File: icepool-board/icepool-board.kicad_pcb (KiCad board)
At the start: 4 copper layers, 131 parts, among them J1 PWR, J2 PWR_IN, J3 I2C, J4 SWD, J5 8P8C_Shielded, J6 8P8C_Shielded, SW1 B3U-1000P, U1 LD1117S33CTR, U2 LD1117S12CTR, U3 ATSAMD21E, U4 ISL83488/ISL83490, U5 iCE40HX8K-BG121(121-Ball_caBG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, U6 iCE40HX8K-BG121(121-Ball_caBG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, X1 ASV-12.000MHz-L??-50, Y1 16MHz

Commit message: Playing with layout a bit more.
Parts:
- removed L1, L2: FB, Inductor_SMD:L_0805_2012Metric
- removed the R13 at (94.1, 125.0)
- removed the R19 at (96.0, 119.0)
- removed the R6 at (83.1, 123.0)
- removed the R7 at (83.1, 127.0)
- added R1: 0R, Jumper:SolderJumper-2_P1.3mm_Open_TrianglePad1.0x1.5mm, F.Cu at (65.0, 154.0)
- added R11: 10k, Resistor_SMD:R_0805_2012Metric, F.Cu at (89.1, 144.2)
- added R14: 10k, Resistor_SMD:R_0805_2012Metric, F.Cu at (94.1, 143.2)
- added R15: 10k, Resistor_SMD:R_0805_2012Metric, F.Cu at (94.1, 140.2)
- added R21: OMIT, Resistor_SMD:R_0805_2012Metric_Pad1.15x1.40mm_HandSolder, F.Cu at (96.0, 134.2)
- added R4: 10k, Resistor_SMD:R_0805_2012Metric, F.Cu at (50.0, 143.5)
- JP1: moved to F.Cu
- R2: value 10k -> 0R; footprint Resistor_SMD:R_0805_2012Metric -> Jumper:SolderJumper-2_P1.3mm_Open_TrianglePad1.0x1.5mm
- R20: renamed from R18; moved to F.Cu
- moved C26 108.7 mm to (77.0, 113.0)
- moved C22 108.6 mm to (77.0, 119.0), turned to 270 degrees
- moved C23 107.8 mm to (75.0, 119.0), turned to 90 degrees
- moved C25 98.5 mm to (77.0, 115.0)
- moved R7 71.9 mm to (41.0, 158.8), turned to 180 degrees
- moved J3 68.8 mm to (37.0, 156.2), turned to 0 degrees
- moved R6 67.0 mm to (41.0, 156.2), turned to 180 degrees
- moved J1 56.1 mm to (105.4, 90.2), turned to 270 degrees
- moved J2 49.5 mm to (95.2, 92.7), turned to 180 degrees
- moved J5 47.0 mm to (68.6, 90.2), turned to 0 degrees
- moved R2 34.1 mm to (87.0, 154.0)
- moved J4 27.4 mm to (78.0, 102.5)
- moved R17 27.2 mm to (70.0, 106.8)
- moved U4 26.5 mm to (44.5, 102.9)
- moved U5 22.4 mm to (74.2, 116.0)
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- renumbered R11 to R13, R14 to R16, R15 to R17, R16 to R18, R17 to R19, R20 to R22, R21 to R23, R22 to R24, R23 to R25, R24 to R26, R25 to R27, R26 to R28, R27 to R29, R1 to R3, R28 to R30, R29 to R31, R30 to R32, R31 to R33, R3 to R5, R4 to R6, R5 to R7
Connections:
- J1 pad 1: /VPWR -> Net-(J1-Pad1)
- J1 pad 2: Net-(J1-Pad2) -> /VPWR
- J4 pad 6: (no net) -> /TDO
- J4 pad 8: (no net) -> /TDI
- J5 pad 1: /TX+ -> /RX+
- J5 pad 2: /TX- -> /RX-
- J5 pad 3: /RX+ -> /TX+
- J5 pad 4: (no net) -> Net-(J5-Pad4)
- J5 pad 5: (no net) -> Net-(J5-Pad5)
- J5 pad 6: /RX- -> /TX-
- J5 pad 7: (no net) -> Net-(J5-Pad7)
- J5 pad 8: (no net) -> Net-(J5-Pad8)
- J6 pad 1: /TX+ -> /RX+
- J6 pad 2: /TX- -> /RX-
- J6 pad 3: /RX+ -> /TX+
- J6 pad 4: (no net) -> Net-(J6-Pad4)
- J6 pad 5: (no net) -> Net-(J6-Pad5)
- J6 pad 6: /RX- -> /TX-
- J6 pad 7: (no net) -> Net-(J6-Pad7)
- J6 pad 8: (no net) -> Net-(J6-Pad8)
- JP1 pad 1: /RX- -> Net-(JP1-Pad1)
- JP1 pad 2: Net-(JP1-Pad2) -> /RX+
- L3 pad 1: Net-(J1-Pad2) -> Net-(J1-Pad1)
- L4 pad 2: /VDDIN -> +3V3
- R10 pad 1: /CRESET_B -> /~READY_ANY
- R12 pad 1: GND -> /CRESET_B
- R12 pad 2: /MOSI -> +3V3
- R2 pad 1: +3V3 -> Net-(R2-Pad1)
- R2 pad 2: /~RESET -> VCC
- R20 pad 1: /RX+ -> Net-(JP1-Pad1)
- R20 pad 2: Net-(JP1-Pad2) -> /RX-
- R3 pad 1: Net-(L2-Pad1) -> +1V2
- R8 pad 1: /~READY_ANY -> /~WE
- R9 pad 1: /~READY_ANY -> /~GS
- U1 pad 2: Net-(L1-Pad1) -> +3V3
- U1 pad 3: VCC -> Net-(R1-Pad1)
- U1 pad 4: Net-(L1-Pad1) -> +3V3
- U2 pad 2: Net-(L2-Pad1) -> +1V2
- U2 pad 3: VCC -> Net-(R2-Pad1)
- U2 pad 4: Net-(L2-Pad1) -> +1V2
- U3 pad 13: (no net) -> Net-(U3-Pad13)
- U3 pad 14: (no net) -> Net-(U3-Pad14)
- U5 pad A1: (no net) -> Net-(U5-PadA1)
- U5 pad A10: (no net) -> Net-(U5-PadA10)
- U5 pad A11: (no net) -> Net-(U5-PadA11)
- U5 pad A2: (no net) -> Net-(U5-PadA2)
- U5 pad A3: (no net) -> Net-(U5-PadA3)
- U5 pad A4: (no net) -> Net-(U5-PadA4)
- U5 pad A5: (no net) -> Net-(U5-PadA5)
- U5 pad A6: (no net) -> Net-(U5-PadA6)
- U5 pad A7: (no net) -> Net-(U5-PadA7)
- U5 pad A8: (no net) -> Net-(U5-PadA8)
- U5 pad A9: (no net) -> Net-(U5-PadA9)
- U5 pad B1: (no net) -> Net-(U5-PadB1)
- U5 pad B10: (no net) -> Net-(U5-PadB10)
- U5 pad B11: (no net) -> Net-(U5-PadB11)
- U5 pad B2: (no net) -> Net-(U5-PadB2)
- U5 pad B3: (no net) -> Net-(U5-PadB3)
- U5 pad B4: (no net) -> Net-(U5-PadB4)
- U5 pad B5: (no net) -> Net-(U5-PadB5)
- U5 pad B6: (no net) -> Net-(U5-PadB6)
- U5 pad B7: (no net) -> Net-(U5-PadB7)
- U5 pad B8: (no net) -> Net-(U5-PadB8)
- U5 pad B9: (no net) -> Net-(U5-PadB9)
- U5 pad C1: (no net) -> Net-(U5-PadC1)
- U5 pad C11: (no net) -> Net-(U5-PadC11)
- U5 pad C2: (no net) -> Net-(U5-PadC2)
- U5 pad C3: (no net) -> Net-(U5-PadC3)
- U5 pad C4: (no net) -> Net-(U5-PadC4)
- U5 pad C5: (no net) -> /ICE40HX8K-BG121_0/GNDPLL1
- U5 pad C7: (no net) -> Net-(U5-PadC7)
- U5 pad C8: (no net) -> Net-(U5-PadC8)
- U5 pad C9: (no net) -> Net-(U5-PadC9)
- U5 pad D1: (no net) -> Net-(U5-PadD1)
- U5 pad D10: (no net) -> Net-(U5-PadD10)
- U5 pad D11: (no net) -> Net-(U5-PadD11)
- U5 pad D2: (no net) -> Net-(U5-PadD2)
- U5 pad D3: (no net) -> Net-(U5-PadD3)
- U5 pad D5: (no net) -> Net-(U5-PadD5)
- U5 pad D7: (no net) -> Net-(U5-PadD7)
- U5 pad D9: (no net) -> Net-(U5-PadD9)
- U5 pad E1: (no net) -> Net-(U5-PadE1)
- U5 pad E10: (no net) -> Net-(U5-PadE10)
- U5 pad E11: (no net) -> Net-(U5-PadE11)
- U5 pad E2: (no net) -> Net-(U5-PadE2)
- U5 pad E3: (no net) -> Net-(U5-PadE3)
- U5 pad E8: (no net) -> Net-(U5-PadE8)
- U5 pad E9: (no net) -> Net-(U5-PadE9)
- U5 pad F1: (no net) -> Net-(U5-PadF1)
- U5 pad F10: (no net) -> Net-(U5-PadF10)
- U5 pad F11: (no net) -> Net-(U5-PadF11)
- U5 pad F2: (no net) -> Net-(U5-PadF2)
- U5 pad F3: (no net) -> Net-(U5-PadF3)
- U5 pad F4: (no net) -> Net-(U5-PadF4)
- U5 pad F9: (no net) -> Net-(U5-PadF9)
- U5 pad G1: (no net) -> Net-(U5-PadG1)
- U5 pad G10: (no net) -> Net-(U5-PadG10)
- U5 pad G11: (no net) -> Net-(U5-PadG11)
- U5 pad G2: (no net) -> Net-(U5-PadG2)
- U5 pad G3: (no net) -> Net-(U5-PadG3)
- U5 pad G8: (no net) -> Net-(U5-PadG8)
- U5 pad G9: (no net) -> Net-(U5-PadG9)
- U5 pad H1: (no net) -> Net-(U5-PadH1)
- U5 pad H10: (no net) -> Net-(U5-PadH10)
- U5 pad H11: (no net) -> Net-(U5-PadH11)
- U5 pad H2: (no net) -> Net-(U5-PadH2)
- U5 pad H3: (no net) -> Net-(U5-PadH3)
- U5 pad H7: (no net) -> Net-(U5-PadH7)
- U5 pad H9: (no net) -> Net-(U5-PadH9)
- U5 pad J1: (no net) -> Net-(U5-PadJ1)
- U5 pad J10: (no net) -> Net-(U5-PadJ10)
- U5 pad J11: (no net) -> Net-(U5-PadJ11)
- U5 pad J2: (no net) -> Net-(U5-PadJ2)
- U5 pad J3: /~GS -> Net-(U5-PadJ3)
- U5 pad J5: (no net) -> Net-(U5-PadJ5)
- U5 pad J7: (no net) -> Net-(U5-PadJ7)
- U5 pad J8: (no net) -> /MOSI
- U5 pad K1: (no net) -> Net-(U5-PadK1)
- U5 pad K11: (no net) -> Net-(U5-PadK11)
- U5 pad K2: (no net) -> Net-(U5-PadK2)
- U5 pad K4: (no net) -> Net-(U5-PadK4)
- U5 pad K5: (no net) -> Net-(U5-PadK5)
- U5 pad K6: /~WE -> Net-(U5-PadK6)
- U5 pad K7: (no net) -> Net-(U5-PadK7)
- U5 pad K9: (no net) -> /ICE40HX8K-BG121_0/GMISO
- U5 pad L2: /MOSI -> Net-(U5-PadL2)
- U5 pad L4: (no net) -> Net-(U5-PadL4)
- U5 pad L5: (no net) -> /~WE
- U5 pad L7: (no net) -> Net-(U5-PadL7)
- U5 pad L8: (no net) -> /~GS
- U6 pad A1: (no net) -> Net-(U6-PadA1)
- U6 pad A10: (no net) -> Net-(U6-PadA10)
- U6 pad A11: (no net) -> Net-(U6-PadA11)
- U6 pad A2: (no net) -> Net-(U6-PadA2)
- U6 pad A3: (no net) -> Net-(U6-PadA3)
- U6 pad A4: (no net) -> Net-(U6-PadA4)
- U6 pad A5: (no net) -> Net-(U6-PadA5)
- U6 pad A6: (no net) -> Net-(U6-PadA6)
- U6 pad A7: (no net) -> Net-(U6-PadA7)
- U6 pad A8: (no net) -> Net-(U6-PadA8)
- U6 pad A9: (no net) -> Net-(U6-PadA9)
- U6 pad B1: (no net) -> Net-(U6-PadB1)
- U6 pad B10: (no net) -> Net-(U6-PadB10)
- U6 pad B11: (no net) -> Net-(U6-PadB11)
- U6 pad B2: (no net) -> Net-(U6-PadB2)
- U6 pad B3: (no net) -> Net-(U6-PadB3)
- U6 pad B4: (no net) -> Net-(U6-PadB4)
- U6 pad B5: (no net) -> Net-(U6-PadB5)
- U6 pad B6: (no net) -> Net-(U6-PadB6)
- U6 pad B7: (no net) -> Net-(U6-PadB7)
- U6 pad B8: (no net) -> Net-(U6-PadB8)
- U6 pad B9: (no net) -> Net-(U6-PadB9)
- U6 pad C1: (no net) -> Net-(U6-PadC1)
- U6 pad C11: (no net) -> Net-(U6-PadC11)
- U6 pad C2: (no net) -> Net-(U6-PadC2)
- U6 pad C3: (no net) -> Net-(U6-PadC3)
- U6 pad C4: (no net) -> Net-(U6-PadC4)
- U6 pad C5: (no net) -> /ICE40HX8K-BG121_1/GNDPLL1
- U6 pad C7: (no net) -> Net-(U6-PadC7)
- U6 pad C8: (no net) -> Net-(U6-PadC8)
- U6 pad C9: (no net) -> Net-(U6-PadC9)
- U6 pad D1: (no net) -> Net-(U6-PadD1)
- U6 pad D10: (no net) -> Net-(U6-PadD10)
- U6 pad D11: (no net) -> Net-(U6-PadD11)
- U6 pad D2: (no net) -> Net-(U6-PadD2)
- U6 pad D3: (no net) -> Net-(U6-PadD3)
- U6 pad D5: (no net) -> Net-(U6-PadD5)
- U6 pad D7: (no net) -> Net-(U6-PadD7)
- U6 pad D9: (no net) -> Net-(U6-PadD9)
- U6 pad E1: (no net) -> Net-(U6-PadE1)
- U6 pad E10: (no net) -> Net-(U6-PadE10)
- U6 pad E11: (no net) -> Net-(U6-PadE11)
- U6 pad E2: (no net) -> Net-(U6-PadE2)
- U6 pad E3: (no net) -> Net-(U6-PadE3)
- U6 pad E8: (no net) -> Net-(U6-PadE8)
- U6 pad E9: (no net) -> Net-(U6-PadE9)
- U6 pad F1: (no net) -> Net-(U6-PadF1)
- U6 pad F10: (no net) -> Net-(U6-PadF10)
- U6 pad F11: (no net) -> Net-(U6-PadF11)
- U6 pad F2: (no net) -> Net-(U6-PadF2)
- U6 pad F3: (no net) -> Net-(U6-PadF3)
- U6 pad F4: (no net) -> Net-(U6-PadF4)
- U6 pad F9: (no net) -> Net-(U6-PadF9)
- U6 pad G1: (no net) -> Net-(U6-PadG1)
- U6 pad G10: (no net) -> Net-(U6-PadG10)
- U6 pad G11: (no net) -> Net-(U6-PadG11)
- U6 pad G2: (no net) -> Net-(U6-PadG2)
- U6 pad G3: (no net) -> Net-(U6-PadG3)
- U6 pad G8: (no net) -> Net-(U6-PadG8)
- U6 pad G9: (no net) -> Net-(U6-PadG9)
- U6 pad H1: (no net) -> Net-(U6-PadH1)
- U6 pad H10: (no net) -> Net-(U6-PadH10)
- U6 pad H11: (no net) -> Net-(U6-PadH11)
- U6 pad H2: (no net) -> Net-(U6-PadH2)
- U6 pad H3: (no net) -> Net-(U6-PadH3)
- U6 pad H7: (no net) -> Net-(U6-PadH7)
- U6 pad H9: (no net) -> Net-(U6-PadH9)
- U6 pad J1: (no net) -> Net-(U6-PadJ1)
- U6 pad J10: (no net) -> Net-(U6-PadJ10)
- U6 pad J11: (no net) -> Net-(U6-PadJ11)
- U6 pad J2: (no net) -> Net-(U6-PadJ2)
- U6 pad J3: /~GS -> Net-(U6-PadJ3)
- U6 pad J5: (no net) -> Net-(U6-PadJ5)
- U6 pad J7: (no net) -> Net-(U6-PadJ7)
- U6 pad J8: (no net) -> /FIFO_0_1
- U6 pad K1: (no net) -> Net-(U6-PadK1)
- U6 pad K11: (no net) -> Net-(U6-PadK11)
- U6 pad K2: (no net) -> Net-(U6-PadK2)
- U6 pad K4: (no net) -> Net-(U6-PadK4)
- U6 pad K5: (no net) -> Net-(U6-PadK5)
- U6 pad K6: /~WE -> Net-(U6-PadK6)
- U6 pad K7: (no net) -> Net-(U6-PadK7)
- U6 pad K9: (no net) -> /ICE40HX8K-BG121_1/GMISO
- U6 pad L2: /FIFO_0_1 -> Net-(U6-PadL2)
- U6 pad L4: (no net) -> Net-(U6-PadL4)
- U6 pad L5: (no net) -> /~WE
- U6 pad L7: (no net) -> Net-(U6-PadL7)
- U6 pad L8: (no net) -> /~GS
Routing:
- net +3V3: vias 0 -> 2
- net (no net): vias 0 -> 15

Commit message: Placed FGPA caps and fanout.
Switched FPGA caps to 0603. May switch everything.

Next: set up OSC and IO buses.
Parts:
- added L1: FB, Inductor_SMD:L_0805_2012Metric, F.Cu at (126.7, 72.3)
- added L2: FB, Inductor_SMD:L_0805_2012Metric, F.Cu at (131.1, 72.3)
- C21, C23, C24, C26, C27, C28, C29, C30, C31, C32, C33, C34, C36, C37, C39, C40, C41, C42, C43, C44, C45, C46: footprint Capacitor_SMD:C_0805_2012Metric -> Capacitor_SMD:C_0603_1608Metric
- D4: moved to B.Cu
- TP1, TP10, TP11, TP12, TP13, TP14, TP15, TP16, TP17, TP18, TP19, TP2, TP20, TP21, TP22, TP23, TP24, TP26, TP3, TP4, TP5, TP6, TP7, TP8, TP9: footprint TestPoint:TestPoint_Pad_D1.5mm -> TestPoint:TestPoint_Pad_D1.0mm
- TP25: footprint TestPoint:TestPoint_Pad_D1.5mm -> TestPoint:TestPoint_Pad_D1.0mm; moved to F.Cu
- moved C21 114.5 mm to (77.2, 118.7), turned to 90 degrees
- moved C32 113.1 mm to (70.9, 116.6)
- moved C24 111.2 mm to (70.9, 115.0)
- moved C29 110.2 mm to (73.8, 115.6), turned to 90 degrees
- moved C28 107.3 mm to (70.9, 118.2)
- moved R24 106.7 mm to (69.2, 120.4), turned to 270 degrees
- moved C27 103.7 mm to (75.4, 115.6), turned to 90 degrees
- moved TP25 102.7 mm to (74.3, 130.9)
- moved C31 99.8 mm to (74.0, 118.0)
- moved R25 98.0 mm to (75.7, 112.0), turned to 90 degrees
- moved C44 97.9 mm to (86.0, 118.0)
- moved C33 95.9 mm to (77.5, 122.2), turned to 90 degrees
- moved C37 94.8 mm to (82.9, 115.0), turned to 180 degrees
- moved C30 94.1 mm to (77.2, 115.6), turned to 270 degrees
- moved R22 93.7 mm to (70.9, 108.4)
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- renumbered L3 to L1, L4 to L2
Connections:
- net Net-(R27-Pad2) renamed /ICE40HX8K-BG121_0/SPI_SS_B
- net Net-(R33-Pad2) renamed /ICE40HX8K-BG121_1/SPI_SS_B
- C25 pad 2: /ICE40HX8K-BG121_0/GNDPLL0 -> /ICE40HX8K-BG121_0/GNDPLL1
- C26 pad 2: /ICE40HX8K-BG121_0/GNDPLL0 -> /ICE40HX8K-BG121_0/GNDPLL1
- C38 pad 2: /ICE40HX8K-BG121_1/GNDPLL0 -> /ICE40HX8K-BG121_1/GNDPLL1
- C39 pad 2: /ICE40HX8K-BG121_1/GNDPLL0 -> /ICE40HX8K-BG121_1/GNDPLL1
- U5 pad J8: /MOSI -> Net-(U5-PadJ8)
- U5 pad K7: Net-(U5-PadK7) -> /MOSI
- U6 pad J8: /FIFO_0_1 -> Net-(U6-PadJ8)
- U6 pad K7: Net-(U6-PadK7) -> /FIFO_0_1
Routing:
- net /MOSI: track 0.00 -> 7.50 mm
- net /ICE40HX8K-BG121_0/VCCIO_0: track 0.00 -> 6.65 mm, vias 0 -> 6
- net /ICE40HX8K-BG121_0/VCC0: track 0.00 -> 5.92 mm, vias 0 -> 4
- net /ICE40HX8K-BG121_0/VCCPLL1: track 0.00 -> 4.74 mm, vias 0 -> 1
- net /ICE40HX8K-BG121_0/GNDPLL1: track 0.00 -> 3.94 mm, vias 0 -> 1
- net /FIFO_0_1: track 0.00 -> 3.92 mm
- net /ICE40HX8K-BG121_0/VCCPLL0: track 0.00 -> 3.75 mm, vias 0 -> 1
- net /ICE40HX8K-BG121_0/GNDPLL0: track 0.00 -> 2.26 mm, vias 0 -> 1
- net /ICE40HX8K-BG121_0/VPP_2V5: track 0.00 -> 2.23 mm, vias 0 -> 1
- net /~WE: track 0.00 -> 2.00 mm
- net /~GS: track 0.00 -> 2.00 mm
- net /OSC: track 0.00 -> 2.00 mm
- net /CRESET_B: track 0.00 -> 2.00 mm
- net /ICE40HX8K-BG121_1/GMISO: track 0.00 -> 1.97 mm
- net /ICE40HX8K-BG121_0/GMISO: track 0.00 -> 1.97 mm
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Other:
- net class Default: clearance 0.2 -> 0.127
- rule trace_clearance: 0.2 -> 0.127

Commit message: Uncommitted layout progress from a while ago...
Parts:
- removed TP17: PA00, TestPoint:TestPoint_Pad_D1.0mm
- removed TP18: PA01, TestPoint:TestPoint_Pad_D1.0mm
- removed TP19: PA02, TestPoint:TestPoint_Pad_D1.0mm
- removed TP20: PA03, TestPoint:TestPoint_Pad_D1.0mm
- removed TP21: PA04, TestPoint:TestPoint_Pad_D1.0mm
- removed TP22: PA05, TestPoint:TestPoint_Pad_D1.0mm
- removed TP23: PA06, TestPoint:TestPoint_Pad_D1.0mm
- removed TP24: PA07, TestPoint:TestPoint_Pad_D1.0mm
- moved J4 26.4 mm to (58.8, 120.5)
- moved R16 25.5 mm to (55.2, 123.8), turned to 180 degrees
- moved U3 19.8 mm to (57.5, 128.4)
- moved Y1 19.4 mm to (59.0, 136.0)
- moved U4 13.4 mm to (53.0, 113.2)
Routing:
- net /~RESET: vias 0 -> 2
- net /~READY_ANY: vias 0 -> 1
- net /~READY_ALL: vias 0 -> 1
- net (no net): vias 12 -> 21

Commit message: More layout work.
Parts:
- removed the L1 at (119.0, 140.0)
- removed the L2 at (131.1, 72.3)
- removed the L2 at (63.4, 102.6)
- added L2: FB, Inductor_SMD:L_0805_2012Metric, F.Cu at (50.0, 105.6)
- JP1, R20: moved to B.Cu
- moved TP26 111.3 mm to (85.8, 138.3)
- moved TP3 106.8 mm to (93.3, 142.2)
- moved TP8 106.8 mm to (82.0, 149.5)
- moved TP9 106.8 mm to (88.8, 142.2)
- moved TP10 106.8 mm to (93.3, 137.7)
- moved TP15 106.8 mm to (88.8, 137.7)
- moved TP16 106.8 mm to (97.9, 137.7)
- moved TP1 106.8 mm to (86.6, 146.8)
- moved TP2 106.8 mm to (91.1, 146.8)
- moved TP4 106.8 mm to (80.2, 154.1)
- moved H3 103.3 mm to (125.0, 120.0)
- moved R33 93.5 mm to (89.8, 107.4), turned to 90 degrees
- moved R32 91.9 mm to (86.1, 109.0), turned to 90 degrees
- moved H4 88.7 mm to (125.0, 85.0)
- moved TP12 86.8 mm to (74.7, 142.5)
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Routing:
- net +3V3: vias 2 -> 4
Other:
- board outline added: 100 x 45 mm

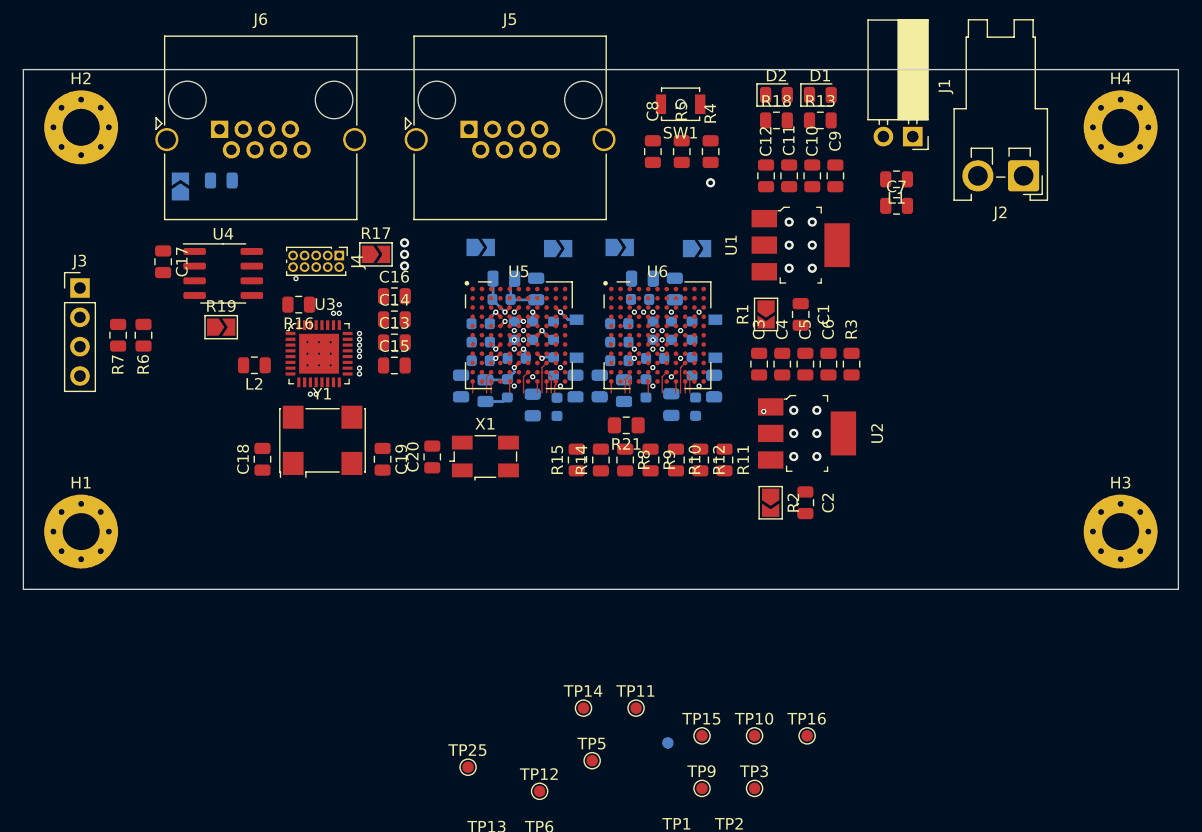
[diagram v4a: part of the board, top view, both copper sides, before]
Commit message: Removed many R0s. Updated layout.
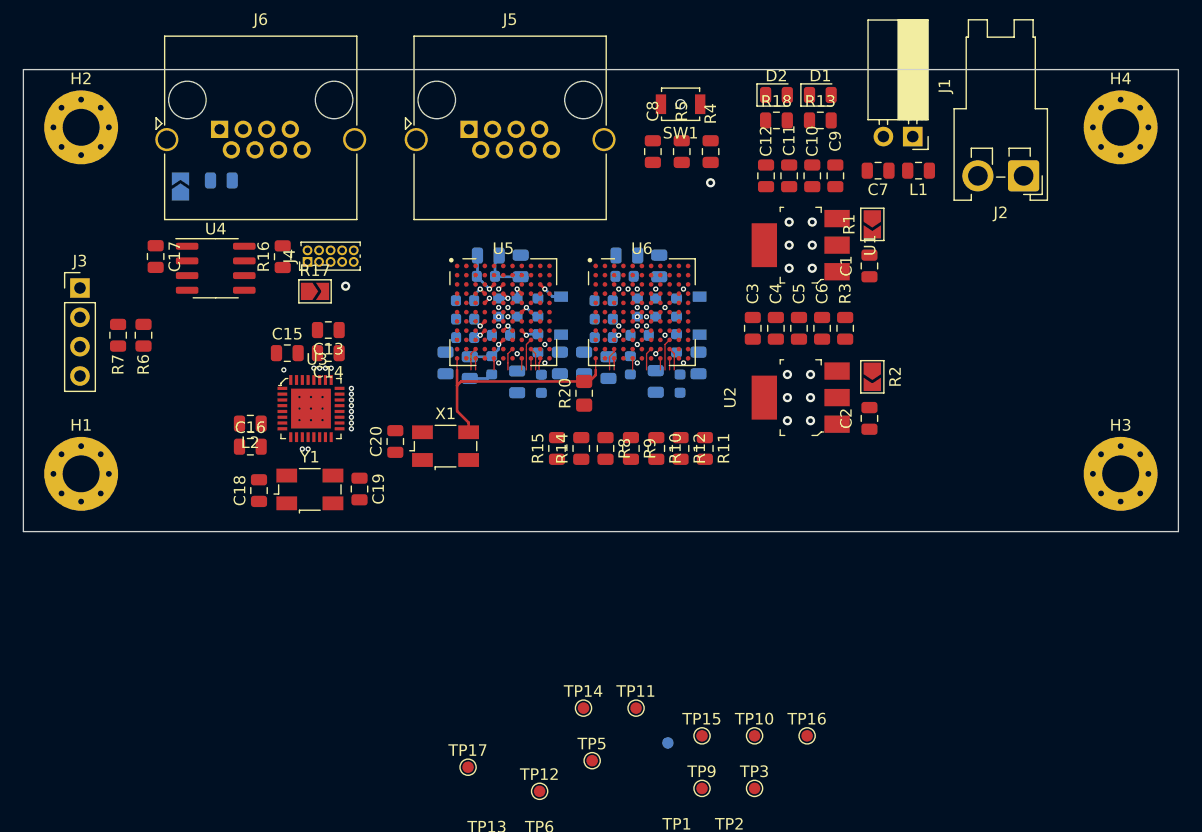
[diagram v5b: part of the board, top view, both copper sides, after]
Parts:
- removed the R19 at (47.1, 102.3)
- removed the R21 at (82.2, 110.8)
- removed the R22 at (69.6, 95.4)
- removed the R23 at (76.3, 95.5)
- removed the R28 at (81.6, 95.4)
- removed R29: 0R, Jumper:SolderJumper-2_P1.3mm_Open_TrianglePad1.0x1.5mm
- added R20: OMIT, Resistor_SMD:R_0805_2012Metric_Pad1.15x1.40mm_HandSolder, F.Cu at (78.5, 108.0)
- Y1: footprint Oscillator:Oscillator_SMD_Abracon_ASV-4Pin_7.0x5.1mm -> Crystal:Crystal_SMD_Abracon_ABM3B-4Pin_5.0x3.2mm
- moved C16 18.0 mm to (49.6, 112.7)
- moved R2 14.0 mm to (103.5, 106.6)
- moved R1 12.1 mm to (103.5, 93.4)
- moved C15 9.33 mm to (52.9, 104.5)
- moved C2 9.17 mm to (103.2, 110.2), turned to 270 degrees
- moved C1 7.28 mm to (103.2, 97.0), turned to 270 degrees
- moved C14 6.43 mm to (56.4, 104.5), turned to 180 degrees
- moved R17 6.17 mm to (55.2, 99.2)
- moved C13 5.82 mm to (56.4, 102.5), turned to 180 degrees
- moved L2 5.06 mm to (49.6, 110.7)
- moved H1 5.00 mm to (35.0, 115.0)
- moved H3 5.00 mm to (125.0, 115.0)
- moved U3 4.80 mm to (55.4, 109.8)
- moved Y1 4.39 mm to (54.8, 116.3)
- moved R16 4.38 mm to (52.5, 96.2), turned to 90 degrees
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- renumbered R20 to R19, R24 to R21, R25 to R22, R26 to R23, R27 to R24, R30 to R25, R31 to R26, R32 to R27, R33 to R28, TP25 to TP17, TP26 to TP18
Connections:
- C15 pad 2: /VDDIN -> +3V3
- C21 pad 2: /ICE40HX8K-BG121_0/VCC0 -> +1V2
- C24 pad 2: /ICE40HX8K-BG121_0/VCC0 -> +1V2
- C27 pad 2: /ICE40HX8K-BG121_0/VCC0 -> +1V2
- C28 pad 2: /ICE40HX8K-BG121_0/VCC0 -> +1V2
- C29 pad 2: /ICE40HX8K-BG121_0/VCCIO_0 -> +3V3
- C30 pad 2: /ICE40HX8K-BG121_0/VCCIO_0 -> +3V3
- C31 pad 2: /ICE40HX8K-BG121_0/VCCIO_0 -> +3V3
- C32 pad 2: /ICE40HX8K-BG121_0/VCCIO_0 -> +3V3
- C33 pad 2: /ICE40HX8K-BG121_0/VCCIO_0 -> +3V3
- C34 pad 2: /ICE40HX8K-BG121_1/VCC0 -> +1V2
- C37 pad 2: /ICE40HX8K-BG121_1/VCC0 -> +1V2
- C40 pad 2: /ICE40HX8K-BG121_1/VCC0 -> +1V2
- C41 pad 2: /ICE40HX8K-BG121_1/VCC0 -> +1V2
- C42 pad 2: /ICE40HX8K-BG121_1/VCCIO_0 -> +3V3
- C43 pad 2: /ICE40HX8K-BG121_1/VCCIO_0 -> +3V3
- C44 pad 2: /ICE40HX8K-BG121_1/VCCIO_0 -> +3V3
- C45 pad 2: /ICE40HX8K-BG121_1/VCCIO_0 -> +3V3
- C46 pad 2: /ICE40HX8K-BG121_1/VCCIO_0 -> +3V3
- U3 pad 30: /VDDIN -> +3V3
- U5 pad D4: /ICE40HX8K-BG121_0/VCC0 -> +1V2
- U5 pad D6: /ICE40HX8K-BG121_0/VCCIO_0 -> +3V3
- U5 pad D8: /ICE40HX8K-BG121_0/VCC0 -> +1V2
- U5 pad E4: /ICE40HX8K-BG121_0/VCCIO_0 -> +3V3
- U5 pad F8: /ICE40HX8K-BG121_0/VCCIO_0 -> +3V3
- U5 pad G4: /ICE40HX8K-BG121_0/VCCIO_0 -> +3V3
- U5 pad H4: /ICE40HX8K-BG121_0/VCC0 -> +1V2
- U5 pad H6: /ICE40HX8K-BG121_0/VCCIO_0 -> +3V3
- U5 pad H8: /ICE40HX8K-BG121_0/VCC0 -> +1V2
- U5 pad L11: /ICE40HX8K-BG121_0/VCCIO_0 -> +3V3
- U6 pad D4: /ICE40HX8K-BG121_1/VCC0 -> +1V2
- U6 pad D6: /ICE40HX8K-BG121_1/VCCIO_0 -> +3V3
- U6 pad D8: /ICE40HX8K-BG121_1/VCC0 -> +1V2
- U6 pad E4: /ICE40HX8K-BG121_1/VCCIO_0 -> +3V3
- U6 pad F8: /ICE40HX8K-BG121_1/VCCIO_0 -> +3V3
- U6 pad G4: /ICE40HX8K-BG121_1/VCCIO_0 -> +3V3
- U6 pad H4: /ICE40HX8K-BG121_1/VCC0 -> +1V2
- U6 pad H6: /ICE40HX8K-BG121_1/VCCIO_0 -> +3V3
- U6 pad H8: /ICE40HX8K-BG121_1/VCC0 -> +1V2
- U6 pad L11: /ICE40HX8K-BG121_1/VCCIO_0 -> +3V3
- Y1 pad 2: /XOUT -> GND
- Y1 pad 3: (no net) -> /XOUT
- Y1 pad 4: (no net) -> GND
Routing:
- net /OSC: track 2.00 -> 20.6 mm
- net +3V3: track 0.00 -> 6.65 mm, vias 4 -> 7
- net /ICE40HX8K-BG121_0/VCCIO_0: track 6.65 -> 0.00 mm, vias 6 -> 1
- net /ICE40HX8K-BG121_0/VCC0: track 5.92 -> 0.00 mm, vias 4 -> 0
- net +1V2: track 0.00 -> 5.92 mm, vias 0 -> 4
- net /MOSI: vias 0 -> 1
- net GND: vias 12 -> 11
- net /~WE: vias 0 -> 1
- net /~RESET: vias 2 -> 0
- net /~READY_ANY: vias 1 -> 0
- net /~READY_ALL: vias 1 -> 0
- net /~GS: vias 0 -> 1
- net /TX: vias 0 -> 1
- net /SDA: vias 0 -> 1
- net /SCL: vias 0 -> 1
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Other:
- board size 100 x 45 mm -> 100 x 40 mm

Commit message: Layout done-ish. Running traces.
Comms bus needs some breathing room... Trying at 6mil.
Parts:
- removed the R20 at (78.5, 108.0)
- removed R21: 120R, Resistor_SMD:R_0805_2012Metric
- removed the R23 at (72.8, 107.0)
- added R14: 10k, Resistor_SMD:R_0805_2012Metric, F.Cu at (60.1, 112.8)
- added R22: 120R, Resistor_SMD:R_0805_2012Metric, B.Cu at (66.5, 105.9)
- added R24: 10k, Resistor_SMD:R_0805_2012Metric, B.Cu at (72.8, 107.0)
- moved R11 32.0 mm to (59.8, 99.8), turned to 90 degrees
- moved R12 27.3 mm to (61.2, 103.6), turned to 90 degrees
- moved R10 26.4 mm to (61.8, 99.8), turned to 90 degrees
- moved R9 22.9 mm to (63.8, 99.8), turned to 90 degrees
- moved R8 18.4 mm to (62.2, 115.7)
- moved R15 17.7 mm to (63.2, 103.6), turned to 270 degrees
- moved R16 14.3 mm to (65.2, 103.6), turned to 270 degrees
- moved C8 5.12 mm to (89.6, 86.7), turned to 90 degrees
- moved R4 4.92 mm to (84.6, 86.7), turned to 270 degrees
- moved C20 4.81 mm to (65.5, 115.7)
- moved X1 4.81 mm to (69.8, 116.1)
- moved R6 4.22 mm to (38.2, 99.4), turned to 270 degrees
- moved C16 1.10 mm to (49.7, 111.5)
- moved L2 1.10 mm to (49.7, 109.5)
- moved R17 0.50 mm to (52.5, 95.7)
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- renumbered R14 to R15, R15 to R16, R16 to R17, R17 to R18, R18 to R19, R19 to R20, R22 to R23, R24 to R25, R25 to R26, R26 to R27, R27 to R28, R28 to R29
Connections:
- R11 pad 1: /~READY_ANY -> /~READY_ALL
- R15 pad 2: /MOSI -> /MISO
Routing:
- net /TX+: track 0.00 -> 48.0 mm
- net /~RESET: track 0.00 -> 47.9 mm, vias 0 -> 2
- net /RX+: track 0.00 -> 42.8 mm
- net /RX-: track 0.00 -> 36.7 mm
- net /TX-: track 0.00 -> 35.7 mm
- net /~READY_ALL: track 1.00 -> 35.0 mm, vias 0 -> 1
- net /SDA: track 0.00 -> 30.6 mm, vias 1 -> 2
- net /SCL: track 0.00 -> 27.6 mm, vias 1 -> 2
- net /RX: track 0.00 -> 26.1 mm, vias 1 -> 0
- net /TX: track 0.00 -> 26.1 mm, vias 1 -> 0
- net /VPWR: track 0.00 -> 16.8 mm
- net /SWDCLK_TCK: track 0.00 -> 15.3 mm
- net VCC: track 0.00 -> 13.0 mm
- net /SWDIO_TMS: track 0.00 -> 12.7 mm, vias 0 -> 1
- net /~READY_ANY: track 1.00 -> 13.2 mm, vias 0 -> 1
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- added copper zone on F.Cu, net +1V2
- added copper zone on F.Cu, net +3V3
- added copper zone on F.Cu, net VCC
